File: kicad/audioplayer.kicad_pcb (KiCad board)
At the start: 2 copper layers, 100 x 75 mm, 34 parts, among them J1 Panel, J2 Charge_USB, J3 Speakers, J4 RFID, SW1 POWER, U1 PB-500, U2 ESP32-nodeMCU, U3 OLED, U4 GY-521, U5 VS1053/SD_breakout, U7 HW-323

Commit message: fix board
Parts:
- added REF**: MountingHole_2.2mm_M2_DIN965, MountingHole:MountingHole_2.2mm_M2_DIN965, F.Cu at (31.7, 112.2)
- added REF**: MountingHole_2.2mm_M2_DIN965, MountingHole:MountingHole_2.2mm_M2_DIN965, F.Cu at (62.6, 110.7)
- added REF**: MountingHole_2.2mm_M2_DIN965, MountingHole:MountingHole_2.2mm_M2_DIN965, F.Cu at (62.6, 97.4)
- added REF**: MountingHole_2.2mm_M2_DIN965, MountingHole:MountingHole_2.2mm_M2_DIN965, F.Cu at (31.7, 95.7)
- moved C7 5.11 mm to (119.8, 50.8), turned to 270 degrees
- moved C6 1.39 mm to (101.7, 106.4)
- moved R9 0.10 mm to (69.7, 92.9)
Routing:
- net GND: track 425.9 -> 463.7 mm, vias 13 -> 14
- net +5V: track 239.4 -> 229.2 mm
- net +3V3: track 152.9 -> 148.2 mm
- net /VCC_AMP: track 59.6 -> 57.7 mm
- net /RST: track 53.1 -> 51.6 mm
- net Net-(J3-Pad2): track 33.7 -> 35.2 mm
- net Net-(J3-Pad1): track 29.9 -> 31.4 mm
- net /ADC_BATT: track 43.0 -> 41.7 mm
- net /SS: track 55.9 -> 54.9 mm
- net /SD_CS: track 41.8 -> 42.5 mm

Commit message: fix board
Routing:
- net /VCC_MP3: track 49.9 -> 42.0 mm
- net GND: track 463.7 -> 456.0 mm
- net +3V3: track 148.2 -> 147.4 mm
- net /AMP_ENABLE: track 19.6 -> 19.0 mm

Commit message: board improvements
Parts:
- removed R4, R6, R8: ?, Resistor_THT:R_Axial_DIN0204_L3.6mm_D1.6mm_P5.08mm_Horizontal
- added REF**: TestPoint_Pad_D1.0mm, TestPoint:TestPoint_Pad_D1.0mm, B.Cu at (92.8, 92.7)
- added REF**: OSHW-Logo2_14.6x12mm_Copper, Symbol:OSHW-Logo2_14.6x12mm_Copper, B.Cu at (47.2, 107.0)
- added REF**: TestPoint_Pad_D1.0mm, TestPoint:TestPoint_Pad_D1.0mm, B.Cu at (87.0, 55.3)
- added REF**: TestPoint_Pad_D1.0mm, TestPoint:TestPoint_Pad_D1.0mm, B.Cu at (90.2, 94.2)
- added REF**: TestPoint_Pad_D1.0mm, TestPoint:TestPoint_Pad_D1.0mm, B.Cu at (88.9, 92.6)
- added REF**: TestPoint_Pad_D1.0mm, TestPoint:TestPoint_Pad_D1.0mm, B.Cu at (88.6, 53.3)
- added REF**: TestPoint_Pad_D1.0mm, TestPoint:TestPoint_Pad_D1.0mm, B.Cu at (90.3, 55.3)
- added U6: ULN2003, Package_DIP:DIP-16_W7.62mm, F.Cu at (42.2, 55.9)
- moved J1 18.0 mm to (39.4, 61.8), turned to 270 degrees
- moved R3 10.4 mm to (36.1, 70.3)
- moved R5 9.79 mm to (33.0, 73.0)
- moved R7 9.44 mm to (34.7, 75.8)
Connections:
- J1 pad 1: LED1 -> /LED3_OD
- J1 pad 10: GND -> +5V
- J1 pad 3: LED2 -> /LED2_OD
- J1 pad 5: LED3 -> /LED1_OD
- J1 pad 9: GND -> +5V
- U2 pad 10: Net-(R4-Pad2) -> LED1
- U2 pad 11: Net-(R6-Pad2) -> LED2
- U2 pad 12: Net-(R8-Pad1) -> LED3
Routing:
- net Net-(R8-Pad1): track 73.0 -> 0.00 mm
- net Net-(R6-Pad2): track 66.7 -> 0.00 mm
- net LED2: track 5.65 -> 55.8 mm
- net LED3: track 7.94 -> 57.8 mm
- net Net-(R4-Pad2): track 49.1 -> 0.00 mm
- net LED1: track 10.3 -> 54.2 mm
- net +3V3: track 147.4 -> 172.2 mm
- net /LED3_OD: track 0.00 -> 18.0 mm
- net SW1: track 57.2 -> 39.7 mm
- net /LED1_OD: track 0.00 -> 16.9 mm
- net /LED2_OD: track 0.00 -> 16.9 mm
- net SW2: track 54.5 -> 39.3 mm
- net Net-(U2-Pad21): track 0.00 -> 13.7 mm
- net SW3: track 52.4 -> 38.8 mm
- net +5V: track 229.1 -> 242.6 mm
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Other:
- net class 5V: via_dia 0.8 -> 1; via_drill 0.4 -> 0.6
- net class Default: via_dia 0.8 -> 1; via_drill 0.4 -> 0.6
- net class GND: via_dia 0.8 -> 1; via_drill 0.4 -> 0.6
- net class VCC_AMP: via_dia 0.8 -> 1; via_drill 0.4 -> 0.6
- net class thicker added: clearance 0.35, trace_width 0.5, via_dia 1, via_drill 0.6
- rule via_min_drill: 0.3 -> 0.6
- rule via_min_size: 0.4 -> 0.8

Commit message: board rev 02
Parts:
- removed the REF** at (92.8, 92.7)
- removed the REF** at (31.7, 95.7)
- removed the REF** at (87.0, 55.3)
- removed the REF** at (90.2, 94.2)
- removed the REF** at (88.9, 92.6)
- removed the REF** at (88.6, 53.3)
- removed the REF** at (90.3, 55.3)
- removed the REF** at (31.7, 112.2)
- removed the REF** at (62.6, 110.7)
- removed the REF** at (62.6, 97.4)
- added R4: 4.7k, Resistor_THT:R_Axial_DIN0204_L3.6mm_D1.6mm_P7.62mm_Horizontal, F.Cu at (43.7, 72.0)
- J1: footprint Connector_PinHeader_2.54mm:PinHeader_2x05_P2.54mm_Vertical -> Connector_PinHeader_2.54mm:PinHeader_2x07_P2.54mm_Vertical
- R1, R2, R3, R5, R7, R9: footprint Resistor_THT:R_Axial_DIN0204_L3.6mm_D1.6mm_P5.08mm_Horizontal -> Resistor_THT:R_Axial_DIN0204_L3.6mm_D1.6mm_P7.62mm_Horizontal
- U2: footprint audioplayer:esp32-nodemcu -> audioplayer:esp32-nodemcu-noholes
- U4: footprint audioplayer:gy-521 -> audioplayer:gy-521-noholes
- moved C3 39.5 mm to (64.8, 61.2)
- moved C5 29.0 mm to (98.3, 46.7), turned to 90 degrees
- moved L1 22.3 mm to (67.6, 46.5), turned to 270 degrees
- moved C2 13.1 mm to (109.5, 111.4), turned to 90 degrees
- moved J1 9.79 mm to (32.6, 68.9), turned to 180 degrees
- moved C7 9.79 mm to (114.5, 59.0), turned to 0 degrees
- moved R3 9.29 mm to (27.4, 73.8), turned to 0 degrees
- moved U2 9.19 mm to (69.7, 79.9), turned to 270 degrees
- moved R5 8.08 mm to (38.7, 78.7), turned to 90 degrees
- moved R7 6.60 mm to (41.1, 77.1), turned to 90 degrees
- moved J4 6.05 mm to (117.7, 76.6)
- moved J3 5.69 mm to (115.9, 90.5), turned to 0 degrees
- moved R9 5.52 mm to (64.9, 95.6)
- moved REF** 5.39 mm to (52.6, 107.8)
- moved C6 4.95 mm to (101.6, 111.4), turned to 90 degrees
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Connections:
- J1 pad 1: /LED3_OD -> +5V
- J1 pad 10: +5V -> Net-(J1-Pad10)
- J1 pad 2: SW3 -> SW4
- J1 pad 3: /LED2_OD -> /LED4_OD
- J1 pad 4: SW2 -> SW3
- J1 pad 5: /LED1_OD -> /LED3_OD
- J1 pad 6: SW1 -> SW2
- J1 pad 7: GND -> /LED2_OD
- J1 pad 8: GND -> SW1
- J1 pad 9: +5V -> /LED1_OD
- U1 pad 7: GND -> Net-(U1-Pad7)
- U2 pad 16: Net-(U2-Pad16) -> LED4
- U2 pad 17: Net-(U2-Pad17) -> LED5
- U2 pad 18: Net-(U2-Pad18) -> LED6
- U2 pad 6: Net-(U2-Pad6) -> SW4
- U6 pad 12: Net-(U6-Pad12) -> Net-(J1-Pad11)
- U6 pad 13: Net-(U6-Pad13) -> /LED1_OD
- U6 pad 14: /LED3_OD -> /LED4_OD
- U6 pad 15: /LED2_OD -> /LED3_OD
- U6 pad 16: /LED1_OD -> /LED2_OD
- U6 pad 2: LED2 -> LED6
- U6 pad 3: LED3 -> LED2
- U6 pad 4: Net-(U6-Pad4) -> LED5
- U6 pad 5: Net-(U6-Pad5) -> LED3
- U6 pad 6: Net-(U6-Pad6) -> LED4
- U6 pad 7: Net-(U6-Pad7) -> GND
- U7 pad 11: Net-(U5-Pad12) -> Net-(U5-Pad11)
- U7 pad 9: Net-(U5-Pad11) -> Net-(U5-Pad12)
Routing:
- net +5V: track 242.6 -> 172.3 mm
- net SW4: track 0.00 -> 64.0 mm
- net +3V3: track 172.2 -> 117.3 mm
- net /AMP_ENABLE: track 19.0 -> 71.8 mm
- net /MOSI: track 76.3 -> 29.7 mm, vias 2 -> 0
- net SW1: track 39.7 -> 82.3 mm
- net /RST: track 51.6 -> 89.1 mm, vias 0 -> 2
- net /MP3_XCS: track 28.2 -> 64.5 mm
- net /ADC_BATT: track 41.7 -> 76.7 mm, vias 0 -> 2
- net SW2: track 39.3 -> 73.4 mm
- net GND: track 468.3 -> 434.3 mm, vias 14 -> 6
- net LED3: track 57.8 -> 24.7 mm
- net /LOW_BATT: track 18.1 -> 47.7 mm, vias 0 -> 2
- net SW3: track 38.8 -> 67.1 mm
- net /SDA: track 67.9 -> 96.1 mm
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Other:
- net class 5V: via_dia 1 -> 1.4
- net class Default: via_dia 1 -> 1.4
- net class GND removed
- net class VCC_AMP removed
- net class thicker removed
- rule via_min_size: 0.8 -> 1.4
- board text added: "MP3-DUCK rev 02"
- board text removed: "MP3-DUCK rev 01"

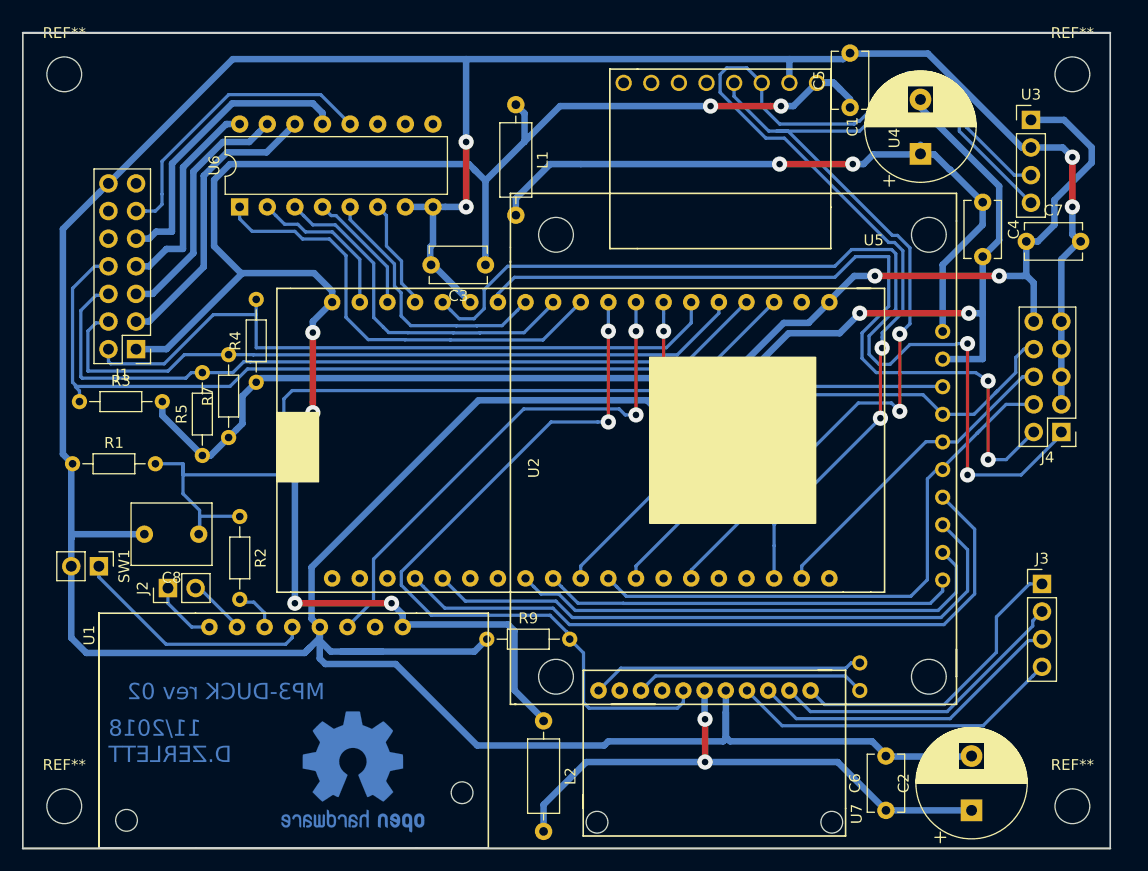
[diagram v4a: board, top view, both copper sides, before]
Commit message: board revision 03
better ground handling, vastly reduced background noise
added reconstruction filter to vs1053 output
added possibillity to add headphone jack
use smd darlington array
add diode for battery low signal
add diode for charging connector (reverse polarity protection just in case)
use 10-pin panel connector and swapped connections for better PCB routing
swapped some GPIO-Pins for better PCB routing (i.e. RFID SS,SCK)
use restor ladder for button GPIOs
removed supply decoupling for SD/MP3 board
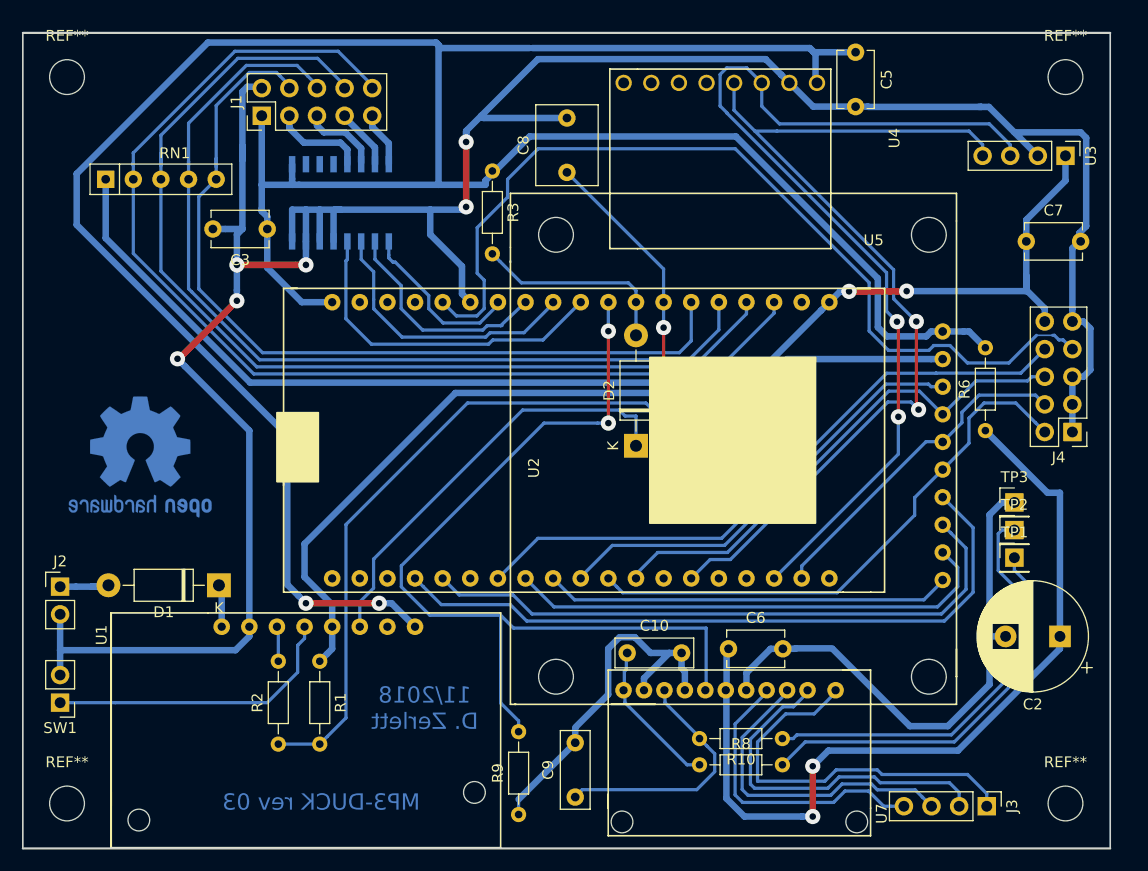
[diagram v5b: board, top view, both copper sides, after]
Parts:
- removed C1: 100u, Capacitor_THT:CP_Radial_D10.0mm_P5.00mm
- removed C4: C, Capacitor_THT:C_Disc_D5.1mm_W3.2mm_P5.00mm
- removed L1, L2: L, Inductor_THT:L_Axial_L6.6mm_D2.7mm_P10.16mm_Horizontal_Vishay_IM-2
- removed R4, R5, R7: 4.7k, Resistor_THT:R_Axial_DIN0204_L3.6mm_D1.6mm_P7.62mm_Horizontal
- added C10: 4.7n, Capacitor_THT:C_Rect_L7.0mm_W2.5mm_P5.00mm, F.Cu at (77.8, 96.9)
- added C9: 4.7n, Capacitor_THT:C_Rect_L7.0mm_W2.5mm_P5.00mm, F.Cu at (73.0, 110.1)
- added D1: 1N4007, Diode_THT:D_DO-41_SOD81_P10.16mm_Horizontal, F.Cu at (40.2, 90.7)
- added D2: 1N4007, Diode_THT:D_DO-41_SOD81_P10.16mm_Horizontal, F.Cu at (78.6, 77.8)
- added R10: 1k, Resistor_THT:R_Axial_DIN0204_L3.6mm_D1.6mm_P7.62mm_Horizontal, F.Cu at (92.1, 104.7)
- added R6: 10, Resistor_THT:R_Axial_DIN0204_L3.6mm_D1.6mm_P7.62mm_Horizontal, F.Cu at (110.7, 76.4)
- added R8: 1k, Resistor_THT:R_Axial_DIN0204_L3.6mm_D1.6mm_P7.62mm_Horizontal, F.Cu at (84.4, 107.2)
- added RN1: R_Network04, Resistor_THT:R_Array_SIP5, F.Cu at (29.8, 53.3)
- added TP1: R, Connector_PinHeader_2.54mm:PinHeader_1x01_P2.54mm_Vertical, F.Cu at (113.4, 88.1)
- added TP2: L, Connector_PinHeader_2.54mm:PinHeader_1x01_P2.54mm_Vertical, F.Cu at (113.4, 85.6)
- added TP3: GNDA, Connector_PinHeader_2.54mm:PinHeader_1x01_P2.54mm_Vertical, F.Cu at (113.4, 83.0)
- C2: value 470u -> 100u
- C6: value C -> 100n
- J1: footprint Connector_PinHeader_2.54mm:PinHeader_2x07_P2.54mm_Vertical -> Connector_PinHeader_2.54mm:PinHeader_2x05_P2.54mm_Vertical
- J3: value Speakers -> SPK
- R3: value 4.7k -> 10k
- U6: footprint Package_DIP:DIP-16_W7.62mm -> Package_SO:SOIC-16W_5.3x10.2mm_P1.27mm; moved to B.Cu
- moved C8 47.5 mm to (72.3, 52.7), turned to 90 degrees
- moved R3 43.5 mm to (65.4, 52.6), turned to 270 degrees
- moved REF** 34.9 mm to (33.0, 78.8)
- moved R1 29.1 mm to (49.5, 97.6), turned to 270 degrees
- moved J1 24.4 mm to (44.2, 47.5), turned to 90 degrees
- moved R2 21.2 mm to (45.7, 105.3), turned to 90 degrees
- moved J3 21.1 mm to (110.9, 111.0), turned to 270 degrees
- moved C6 20.7 mm to (87.1, 96.5), turned to 0 degrees
- moved C3 20.3 mm to (44.7, 57.9)
- moved C2 17.9 mm to (117.6, 95.4), turned to 180 degrees
- moved R9 16.4 mm to (67.8, 111.7), turned to 90 degrees
- moved SW1 13.0 mm to (25.6, 101.4), turned to 180 degrees
- moved J2 9.92 mm to (25.6, 90.8), turned to 0 degrees
- moved U6 9.28 mm to (51.4, 55.5)
- moved C5 5.11 mm to (98.8, 41.6), turned to 270 degrees
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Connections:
- net /VCC_AMP renamed +5VA
- C2 pad 2: GND -> GNDA
- C6 pad 2: GND -> GNDA
- J1 pad 10: Net-(J1-Pad10) -> SW1
- J1 pad 2: SW4 -> GND
- J1 pad 4: SW3 -> SW4
- J1 pad 6: SW2 -> SW3
- J1 pad 8: SW1 -> SW2
- J2 pad 1: Net-(J2-Pad1) -> Net-(D1-Pad2)
- J2 pad 2: Net-(J2-Pad2) -> GND
- J4 pad 1: /RST -> GND
- J4 pad 2: /SS -> /SCK
- J4 pad 4: /SCK -> /MOSI
- J4 pad 6: /MOSI -> /MISO
- J4 pad 7: GND -> /RST
- J4 pad 8: /MISO -> /SS
- R3 pad 1: SW1 -> +5V
- R3 pad 2: +3V3 -> Net-(D2-Pad2)
- R9 pad 1: GND -> GNDA
- U1 pad 1: Net-(J2-Pad1) -> Net-(D1-Pad1)
- U1 pad 2: Net-(J2-Pad2) -> GND
- U2 pad 13: /SS -> LED4
- U2 pad 16: LED4 -> Net-(U2-Pad16)
- U2 pad 17: LED5 -> Net-(U2-Pad17)
- U2 pad 18: LED6 -> Net-(U2-Pad18)
- U2 pad 26: Net-(U2-Pad26) -> /SS
- U2 pad 8: /LOW_BATT -> Net-(D2-Pad2)
- U5 pad 1: /VCC_MP3 -> +5V
- U6 pad 1: LED1 -> LED4
- U6 pad 12: Net-(J1-Pad11) -> Net-(U6-Pad12)
- U6 pad 13: /LED1_OD -> /LED4_OD
- U6 pad 14: /LED4_OD -> /LED3_OD
- U6 pad 15: /LED3_OD -> /LED2_OD
- U6 pad 16: /LED2_OD -> /LED1_OD
- U6 pad 2: LED6 -> LED3
- U6 pad 4: LED5 -> LED1
- U6 pad 5: LED3 -> GND
- U6 pad 6: LED4 -> GND
- U6 pad 9: Net-(U6-Pad9) -> +5V
- U7 pad 10: Net-(U7-Pad10) -> GNDA
- U7 pad 11: Net-(U5-Pad11) -> Net-(C10-Pad1)
- U7 pad 5: GND -> GNDA
- U7 pad 8: Net-(U7-Pad8) -> GNDA
- U7 pad 9: Net-(U5-Pad12) -> Net-(C9-Pad1)
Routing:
- net GNDA: track 0.00 -> 113.0 mm
- net GND: track 434.3 -> 322.5 mm
- net +5V: track 172.3 -> 255.8 mm, vias 6 -> 2
- net /VCC_MP3: track 62.2 -> 0.00 mm, vias 2 -> 0
- net Net-(R10-Pad1): track 0.00 -> 39.5 mm
- net Net-(R8-Pad2): track 0.00 -> 37.0 mm
- net Net-(J1-Pad11): track 28.1 -> 0.00 mm
- net +5VA: track 51.9 -> 79.0 mm
- net Net-(U5-Pad11): track 25.1 -> 0.00 mm
- net Net-(C9-Pad1): track 0.00 -> 23.0 mm
- net /LED1_OD: track 27.2 -> 5.33 mm
- net SW2: track 73.4 -> 94.9 mm
- net SW1: track 82.3 -> 103.6 mm
- net Net-(U5-Pad12): track 21.2 -> 0.00 mm
- net /LED4_OD: track 28.1 -> 8.89 mm
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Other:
- board text added: "11/2018 D. Zerlett"
- board text added: "MP3-DUCK rev 03"
- board text removed: "11/2018 D.ZERLETT"
- board text removed: "MP3-DUCK rev 02"
